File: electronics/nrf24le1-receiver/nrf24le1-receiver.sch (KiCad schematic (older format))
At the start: 19 parts, among them K1 CONN_3, K2 CONN_3, K3 CONN_3, K4 CONN_3, P1 CONN_1, P2 CONN_1, P3 CONN_1, SW1 BIND, U1 MCP1703, U2 NRF24LE1-MODULE-15X21

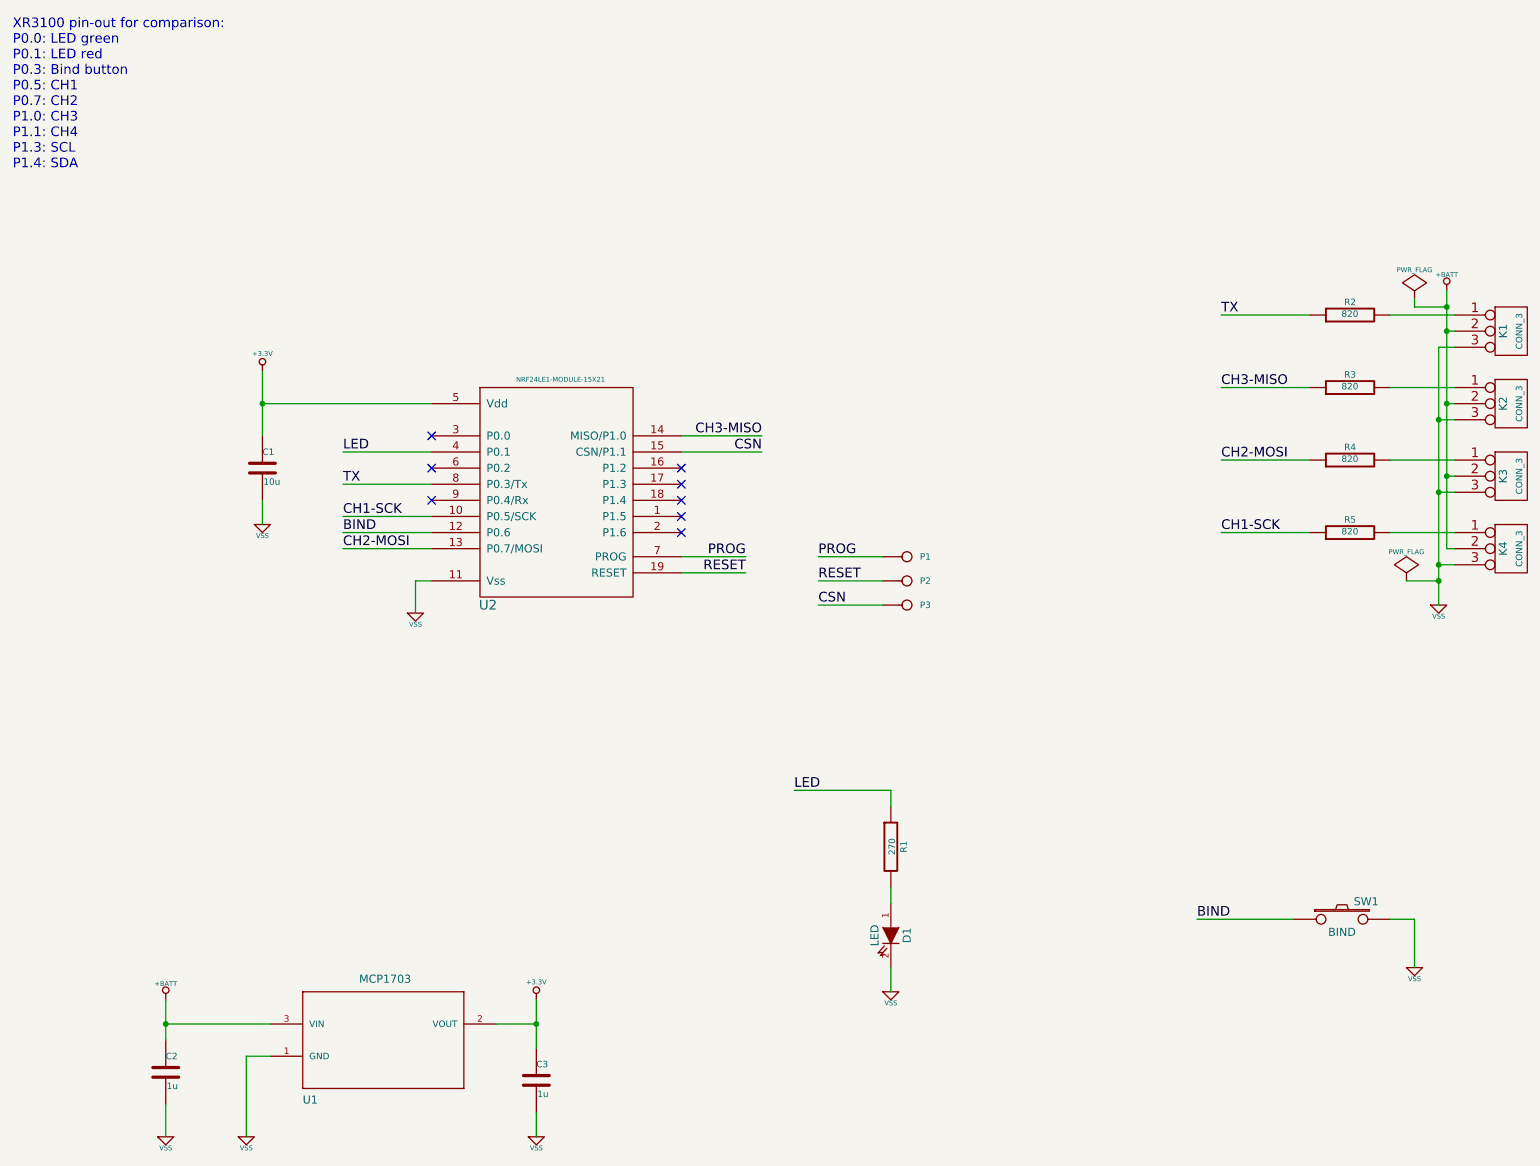
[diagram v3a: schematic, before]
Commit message: Finalize boards and make combined Gerbers for manufacturing
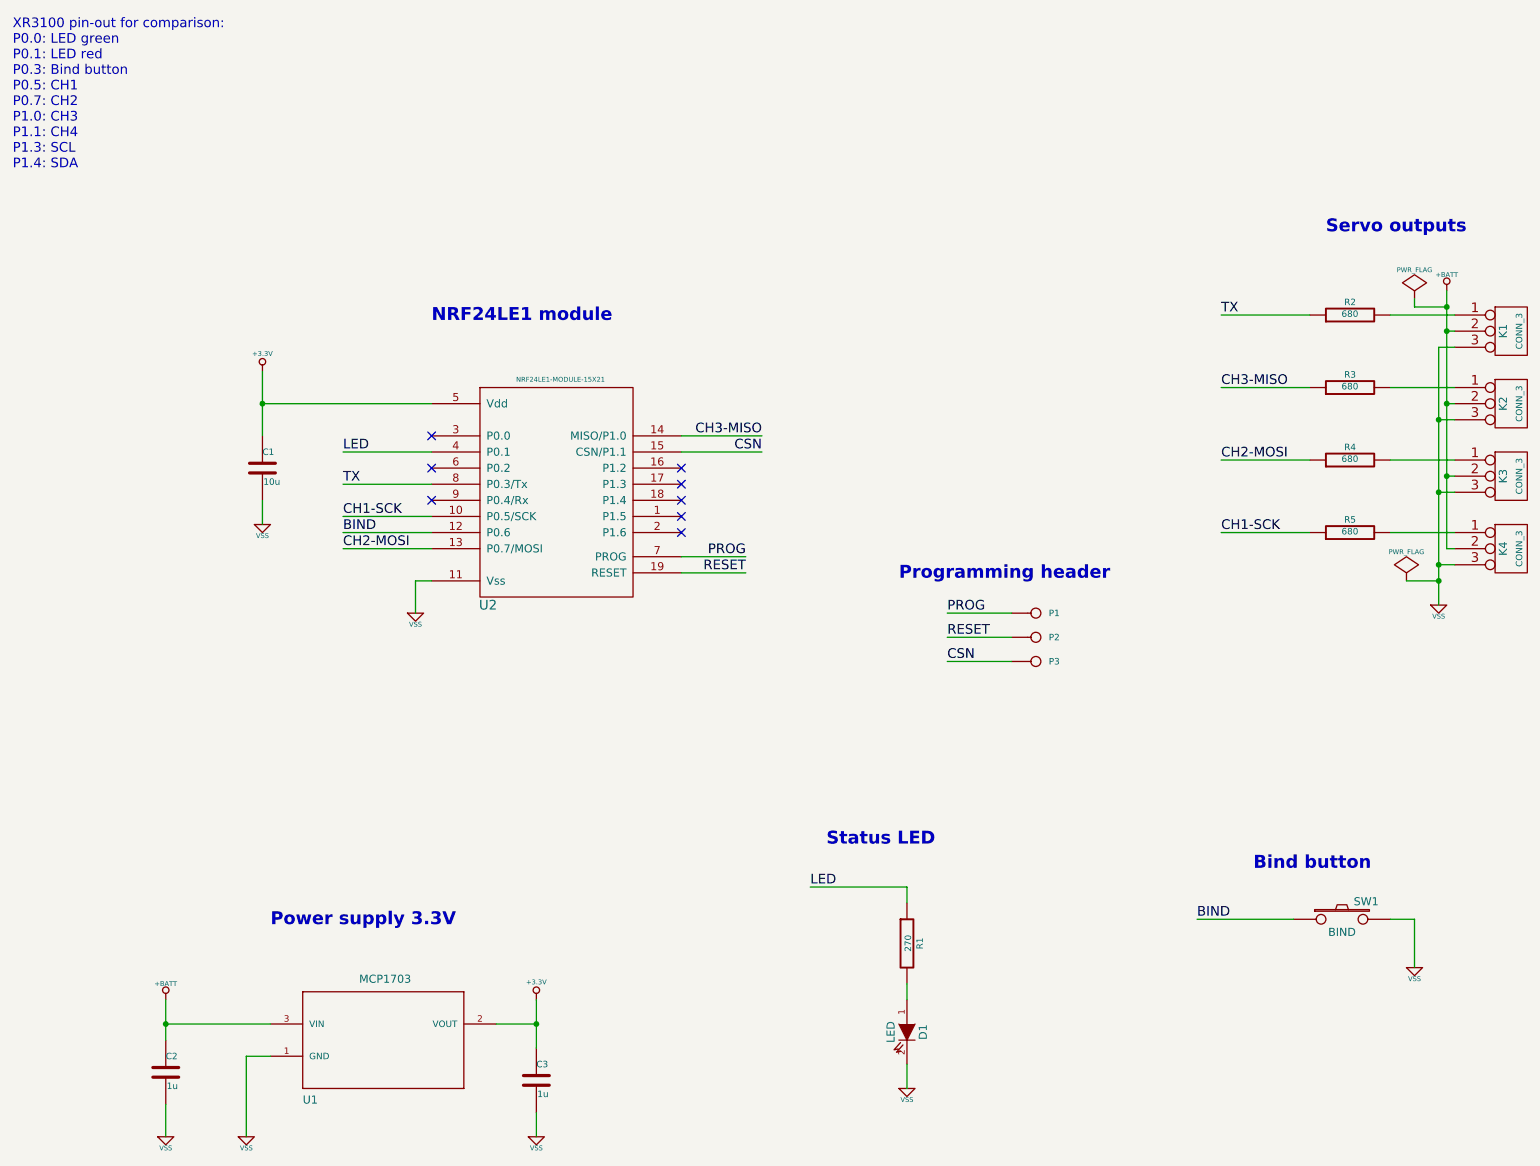
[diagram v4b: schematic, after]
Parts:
- R2, R3, R4, R5: value 820 -> 680
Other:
- note added: "Bind button"
- note added: "NRF24LE1 module"
- note added: "Power supply 3.3V"
- note added: "Programming header"
- note added: "Servo outputs"
- note added: "Status LED"
- moved on the sheet: D1, P1, P2, P3, R1
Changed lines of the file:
@@
 Sheet 1 1
 Title ""
-Date "29 nov 2014"
+Date "30 nov 2014"
 Rev ""
 Comp ""
@@
 P 9050 1650
 F 0 "R2" V 9130 1650 40  0000 C CNN
-F 1 "820" V 9057 1651 40  0000 C CNN
+F 1 "680" V 9057 1651 40  0000 C CNN
 F 2 "~" V 8980 1650 30  0000 C CNN
 F 3 "~" H 9050 1650 30  0000 C CNN
@@
 P 9050 2100
 F 0 "R3" V 9130 2100 40  0000 C CNN
-F 1 "820" V 9057 2101 40  0000 C CNN
+F 1 "680" V 9057 2101 40  0000 C CNN
 F 2 "~" V 8980 2100 30  0000 C CNN
 F 3 "~" H 9050 2100 30  0000 C CNN
@@
 P 9050 2550
 F 0 "R4" V 9130 2550 40  0000 C CNN
-F 1 "820" V 9057 2551 40  0000 C CNN
+F 1 "680" V 9057 2551 40  0000 C CNN
 F 2 "~" V 8980 2550 30  0000 C CNN
 F 3 "~" H 9050 2550 30  0000 C CNN
@@
 P 9050 3000
 F 0 "R5" V 9130 3000 40  0000 C CNN
-F 1 "820" V 9057 3001 40  0000 C CNN
+F 1 "680" V 9057 3001 40  0000 C CNN
 F 2 "~" V 8980 3000 30  0000 C CNN
 F 3 "~" H 9050 3000 30  0000 C CNN
@@
 L LED D1
 U 1 1 547928FB
-P 6200 5500
-F 0 "D1" H 6200 5600 50  0000 C CNN
-F 1 "LED" H 6200 5400 50  0000 C CNN
-F 2 "~" H 6200 5500 60  0000 C CNN
-F 3 "~" H 6200 5500 60  0000 C CNN
-	1    6200 5500
+P 6300 6100
+F 0 "D1" H 6300 6200 50  0000 C CNN
+F 1 "LED" H 6300 6000 50  0000 C CNN
+F 2 "~" H 6300 6100 60  0000 C CNN
+F 3 "~" H 6300 6100 60  0000 C CNN
+	1    6300 6100
 	0    1    1    0
 $EndComp
@@
 L R R1
 U 1 1 5479290A
-P 6200 4950
-F 0 "R1" V 6280 4950 40  0000 C CNN
-F 1 "270" V 6207 4951 40  0000 C CNN
-F 2 "~" V 6130 4950 30  0000 C CNN
-F 3 "~" H 6200 4950 30  0000 C CNN
-	1    6200 4950
+P 6300 5550
+F 0 "R1" V 6380 5550 40  0000 C CNN
+F 1 "270" V 6307 5551 40  0000 C CNN
+F 2 "~" V 6230 5550 30  0000 C CNN
+F 3 "~" H 6300 5550 30  0000 C CNN
+	1    6300 5550
 	1    0    0    -1
 $EndComp
@@
 L VSS #PWR012
 U 1 1 5479294B
-P 6200 5850
-F 0 "#PWR012" H 6200 5850 30  0001 C CNN
-F 1 "VSS" H 6200 5780 30  0000 C CNN
-F 2 "" H 6200 5850 60  0000 C CNN
-F 3 "" H 6200 5850 60  0000 C CNN
-	1    6200 5850
-	1    0    0    -1
-$EndComp
-Text Label 5600 4600 0    60   ~ 0
+P 6300 6450
+F 0 "#PWR012" H 6300 6450 30  0001 C CNN
+F 1 "VSS" H 6300 6380 30  0000 C CNN
+F 2 "" H 6300 6450 60  0000 C CNN
+F 3 "" H 6300 6450 60  0000 C CNN
+	1    6300 6450
+	1    0    0    -1
+$EndComp
+Text Label 5700 5200 0    60   ~ 0
 LED
 Text Label 2800 2500 0    60   ~ 0
@@
 L CONN_1 P1
 U 1 1 54796D23
-P 6300 3150
-F 0 "P1" H 6380 3150 40  0000 L CNN
-F 1 "CONN_1" H 6300 3205 30  0001 C CNN
-F 2 "" H 6300 3150 60  0000 C CNN
-F 3 "" H 6300 3150 60  0000 C CNN
-	1    6300 3150
+P 7100 3500
+F 0 "P1" H 7180 3500 40  0000 L CNN
+F 1 "CONN_1" H 7100 3555 30  0001 C CNN
+F 2 "" H 7100 3500 60  0000 C CNN
+F 3 "" H 7100 3500 60  0000 C CNN
+	1    7100 3500
 	1    0    0    -1
 $EndComp
@@
 L CONN_1 P2
 U 1 1 54796D32
-P 6300 3300
-F 0 "P2" H 6380 3300 40  0000 L CNN
-F 1 "CONN_1" H 6300 3355 30  0001 C CNN
-F 2 "" H 6300 3300 60  0000 C CNN
-F 3 "" H 6300 3300 60  0000 C CNN
-	1    6300 3300
-	1    0    0    -1
-$EndComp
-Text Label 5750 3150 0    60   ~ 0
+P 7100 3650
+F 0 "P2" H 7180 3650 40  0000 L CNN
+F 1 "CONN_1" H 7100 3705 30  0001 C CNN
+F 2 "" H 7100 3650 60  0000 C CNN
+F 3 "" H 7100 3650 60  0000 C CNN
+	1    7100 3650
+	1    0    0    -1
+$EndComp
+Text Label 6550 3500 0    60   ~ 0
 PROG
-Text Label 5750 3300 0    60   ~ 0
+Text Label 6550 3650 0    60   ~ 0
 RESET
 $Comp
 L CONN_1 P3
 U 1 1 54797ABF
-P 6300 3450
-F 0 "P3" H 6380 3450 40  0000 L CNN
-F 1 "CONN_1" H 6300 3505 30  0001 C CNN
-F 2 "" H 6300 3450 60  0000 C CNN
-F 3 "" H 6300 3450 60  0000 C CNN
-	1    6300 3450
-	1    0    0    -1
-$EndComp
-Text Label 5750 3450 0    60   ~ 0
+P 7100 3800
+F 0 "P3" H 7180 3800 40  0000 L CNN
+F 1 "CONN_1" H 7100 3855 30  0001 C CNN
+F 2 "" H 7100 3800 60  0000 C CNN
+F 3 "" H 7100 3800 60  0000 C CNN
+	1    7100 3800
+	1    0    0    -1
+$EndComp
+Text Label 6550 3800 0    60   ~ 0
 CSN
 Wire Wire Line
@@
 	2800 3000 3350 3000
 Wire Wire Line
-	6200 5200 6200 5300
-Wire Wire Line
-	6200 5700 6200 5850
-Wire Wire Line
-	6200 4700 6200 4600
-Wire Wire Line
-	6200 4600 5600 4600
-Wire Wire Line
-	6150 3150 5750 3150
-Wire Wire Line
-	5750 3300 6150 3300
-Wire Wire Line
-	5750 3450 6150 3450
+	6300 5800 6300 5900
+Wire Wire Line
+	6300 6300 6300 6450
+Wire Wire Line
+	6300 5300 6300 5200
+Wire Wire Line
+	6300 5200 5700 5200
+Wire Wire Line
+	6950 3500 6550 3500
+Wire Wire Line
+	6550 3650 6950 3650
+Wire Wire Line
+	6550 3800 6950 3800
 $Comp
 L PWR_FLAG #FLG013
@@
 	2800 2500 3350 2500
 NoConn ~ 3350 2600
+Text Notes 3350 1700 0    80   ~ 16
+NRF24LE1 module
+Text Notes 6250 3300 0    80   ~ 16
+Programming header
+Text Notes 8900 1150 0    80   ~ 16
+Servo outputs
+Text Notes 5800 4950 0    80   ~ 16
+Status LED
+Text Notes 2350 5450 0    80   ~ 16
+Power supply 3.3V
+Text Notes 8450 5100 0    80   ~ 16
+Bind button
 $EndSCHEMATC
